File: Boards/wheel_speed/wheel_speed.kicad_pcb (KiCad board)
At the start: 2 copper layers, 38.1 x 50.8 mm, 41 parts, among them J1 CONN_02X03, J2 MM_F_RA_08, U1 MCP2561-E_SN, U101 TPS560430YF, U2 ATMEGA16M1, Y1 Crystal_SMD

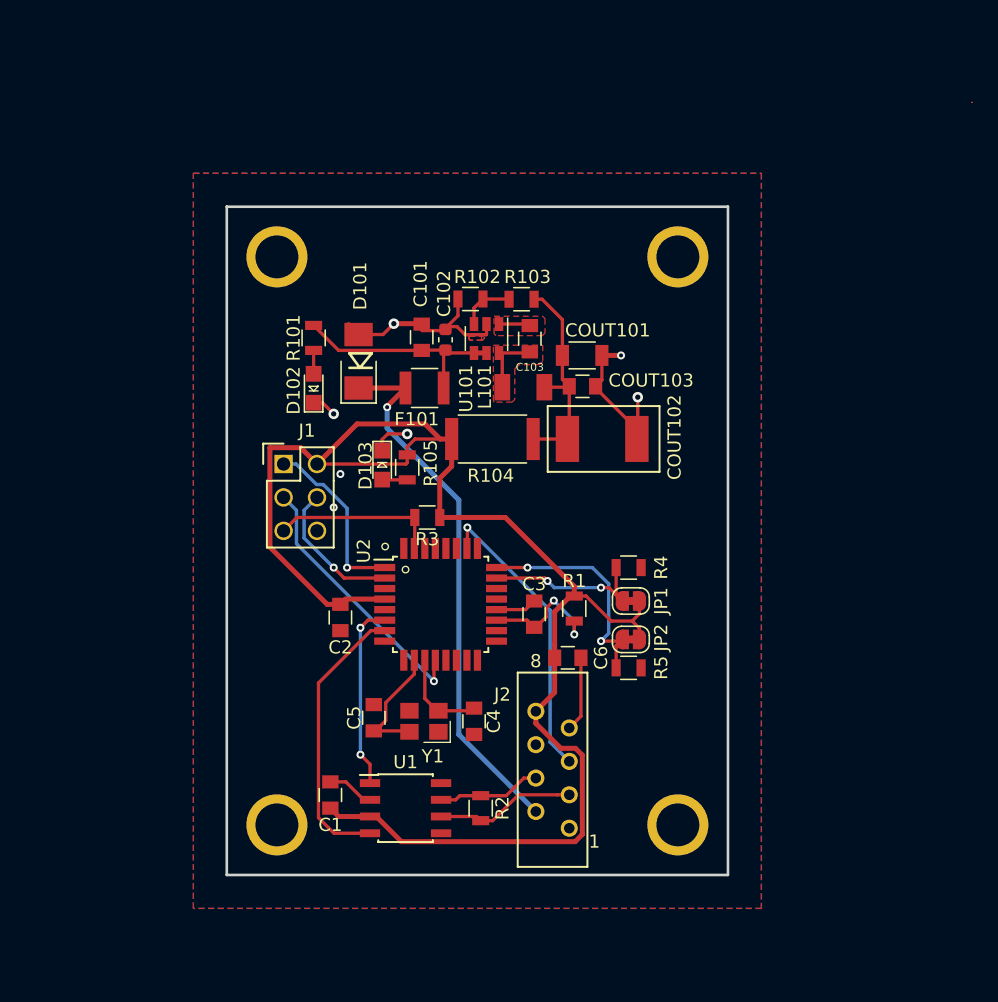
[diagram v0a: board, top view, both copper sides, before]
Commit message: More clear labeling for the jumpers
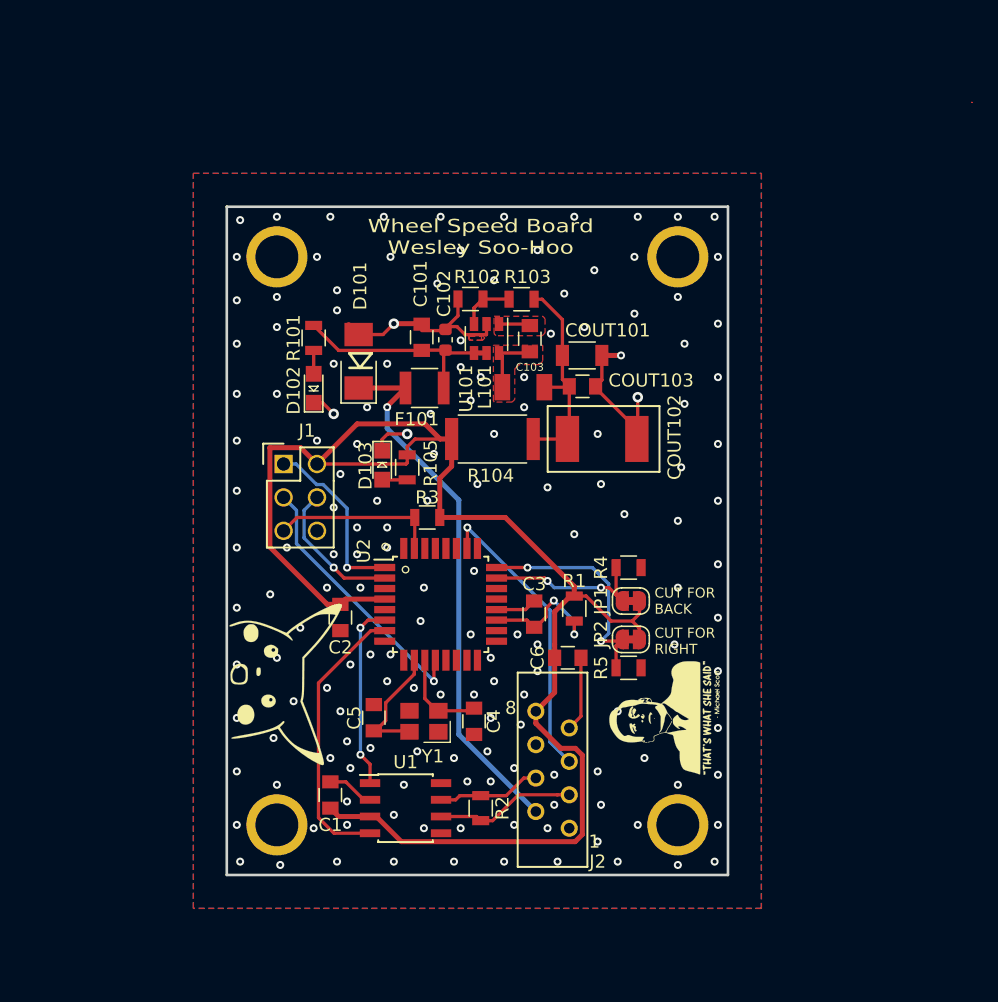
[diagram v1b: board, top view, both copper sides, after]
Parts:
- removed the G*** at (172.7, 91.4)
- added G***: LOGO, img:surprised_pika, F.Cu at (105.4, 112.3)
- added G***: LOGO, img:michael_scott, F.Cu at (134.9, 115.1)
- moved G*** 34.3 mm to (110.0, 100.8), turned to 270 degrees
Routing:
- net GND: vias 7 -> 160
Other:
- board text added: "CUT FOR BACK"
- board text added: "CUT FOR RIGHT"
- board text added: "Wheel Speed Board Wesley Soo-Hoo"

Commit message: Add extra debug lights and redo silkscreen
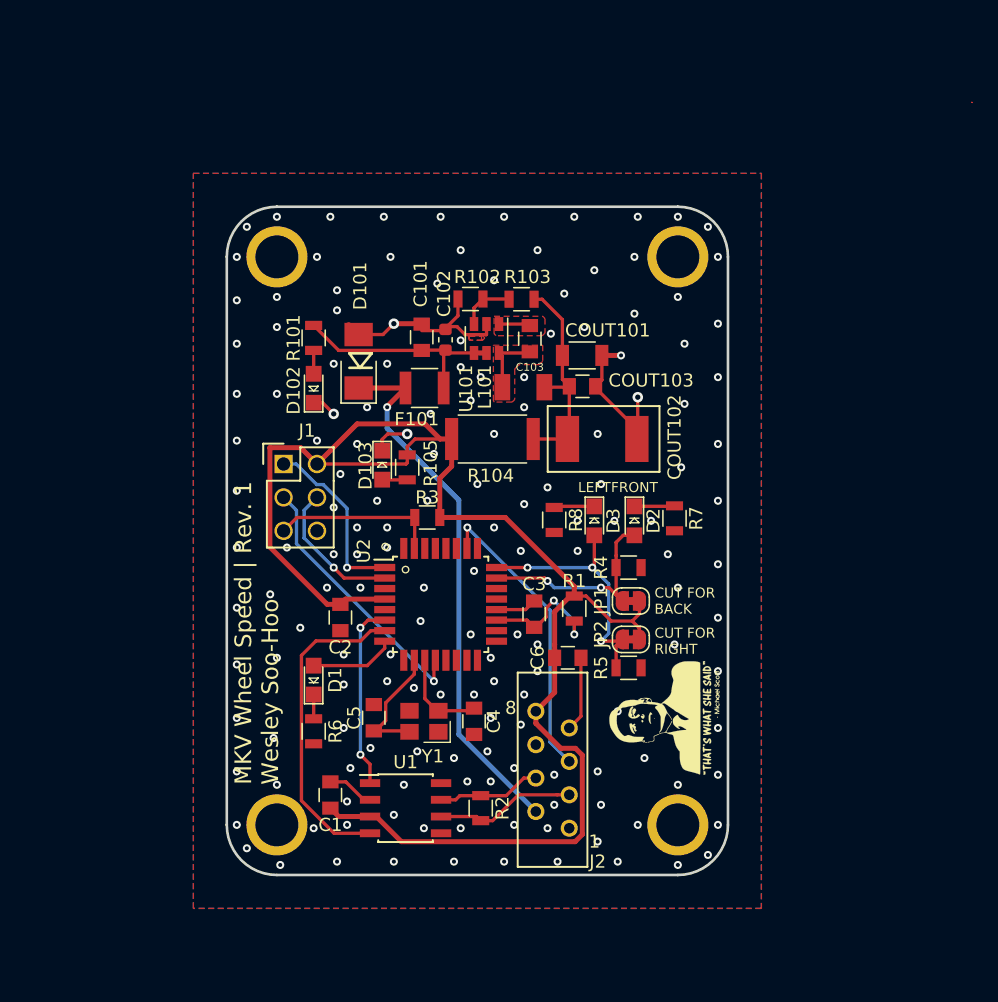
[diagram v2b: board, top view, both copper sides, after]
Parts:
- removed the G*** at (105.4, 112.3)
- added D1: LED_0805, footprints:LED_0805_OEM, F.Cu at (108.2, 112.2)
- added D2: LED_0805, footprints:LED_0805_OEM, F.Cu at (132.6, 100.1)
- added D3: LED_0805, footprints:LED_0805_OEM, F.Cu at (129.5, 100.1)
- added R6: R_120, footprints:R_0805_OEM, F.Cu at (108.2, 116.1)
- added R7: R_120, footprints:R_0805_OEM, F.Cu at (135.6, 99.9)
- added R8: R_120, footprints:R_0805_OEM, F.Cu at (126.5, 100.0)
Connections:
- U2 pad 8: Net-(U2-Pad8) -> /DEBUG
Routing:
- net /DEBUG: track 0.00 -> 6.48 mm
- net /FRONT_SENSE: track 13.0 -> 16.6 mm
- net Net-(D3-Pad1): track 0.00 -> 3.08 mm
- net Net-(D2-Pad1): track 0.00 -> 3.06 mm
- net /CAN_RX: track 21.3 -> 24.4 mm
- net /LEFT_SENSE: track 17.7 -> 20.2 mm, vias 2 -> 3
- net Net-(D1-Pad1): track 0.00 -> 1.84 mm
- net GND: vias 160 -> 161
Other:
- outline, holes or cut-outs redrawn
- board text added: "FRONT"
- board text added: "LEFT"
- board text added: "MKV Wheel Speed | Rev. 1 Wesley Soo-Hoo"
- board text removed: "Wheel Speed Board Wesley Soo-Hoo"

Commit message: fix pinout and move microfit connector to edge of board
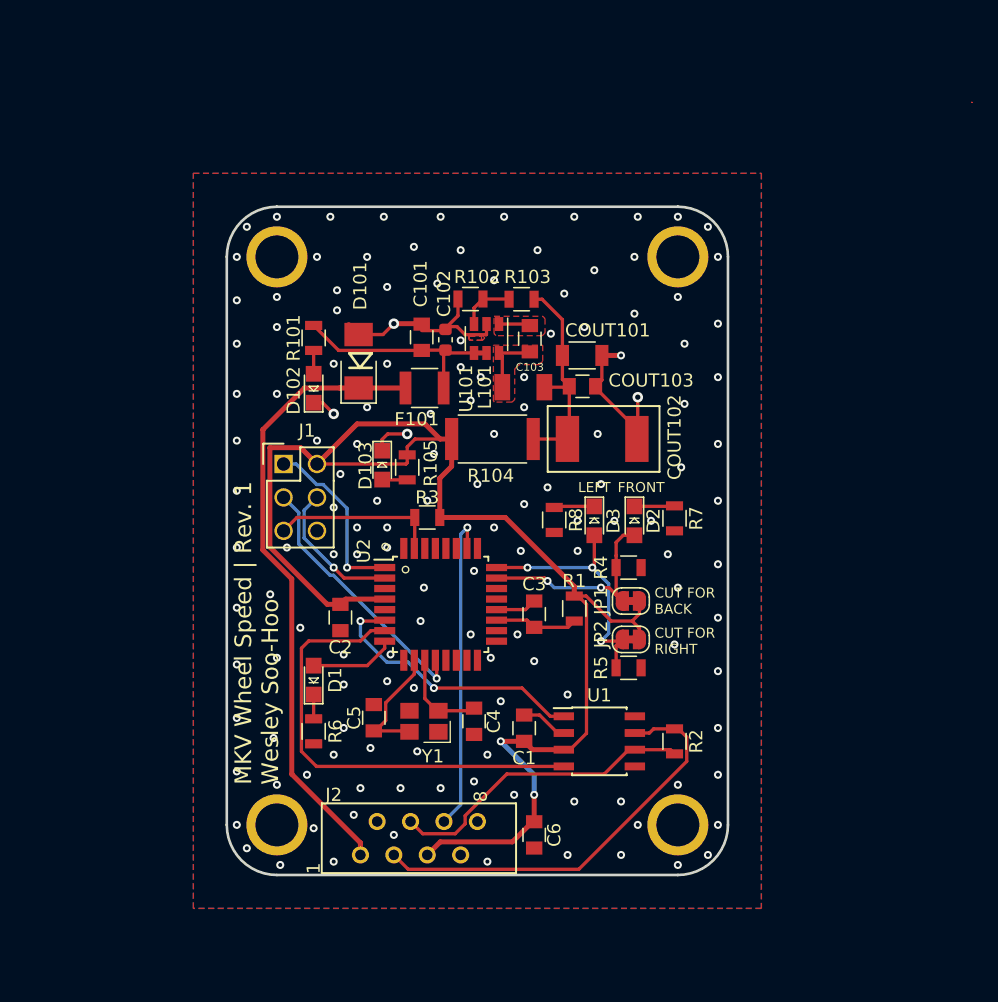
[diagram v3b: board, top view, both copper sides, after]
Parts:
- removed the G*** at (134.9, 115.1)
- moved C1 15.6 mm to (124.2, 115.8)
- moved R2 15.6 mm to (135.6, 116.8)
- moved U1 15.6 mm to (129.9, 116.8)
- moved C6 13.7 mm to (125.0, 124.0), turned to 90 degrees
- moved J2 12.9 mm to (116.8, 125.5), turned to 90 degrees
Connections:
- C6 pad 1: VCC -> GND
- C6 pad 2: GND -> VCC
- J2 pad 1: GND -> /12V
- J2 pad 2: /12V -> GND
- J2 pad 3: /CAN_LO -> /CAN_HI
- J2 pad 4: /CAN_HI -> /CAN_LO
- J2 pad 5: /SENSE_IN -> VCC
- J2 pad 6: GND -> /SENSE_IN
- J2 pad 8: VCC -> GND
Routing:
- net /CAN_HI: track 7.89 -> 32.3 mm
- net /CAN_LO: track 10.7 -> 23.6 mm
- net /CAN_RX: track 24.4 -> 35.1 mm
- net VCC: track 116.5 -> 109.1 mm, vias 0 -> 2
- net /CAN_TX: track 14.2 -> 21.0 mm
- net /12V: track 41.3 -> 47.9 mm, vias 1 -> 0
- net GND: track 44.8 -> 39.1 mm, vias 161 -> 144
- net Net-(C3-Pad1): track 10.0 -> 6.33 mm, vias 2 -> 0
- net /SENSE_IN: track 22.6 -> 24.7 mm

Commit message: Switch to normally open jumpers, rearrange bottom traces
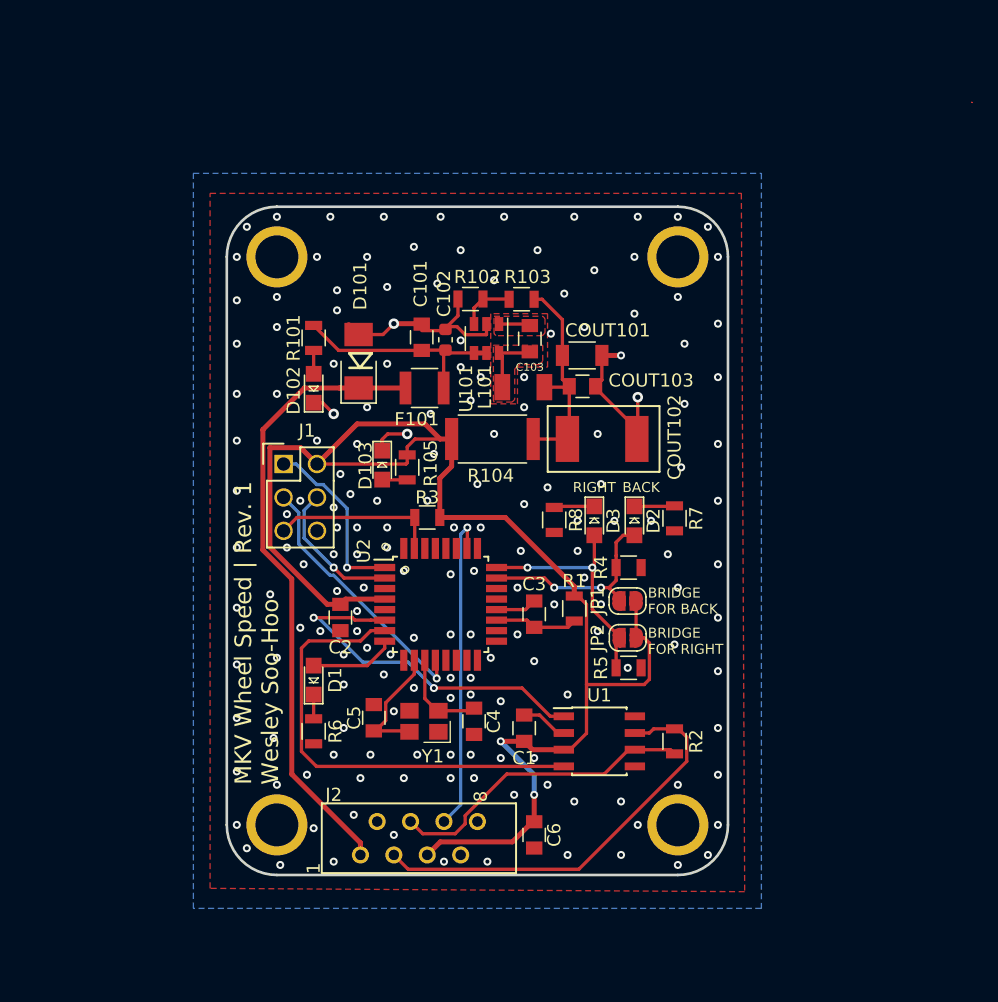
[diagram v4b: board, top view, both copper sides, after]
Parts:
- JP1, JP2: footprint Jumper:SolderJumper-2_P1.3mm_Bridged_RoundedPad1.0x1.5mm -> Jumper:SolderJumper-2_P1.3mm_Open_RoundedPad1.0x1.5mm
- moved JP2 0.27 mm to (132.1, 109.0)
- moved JP1 0.25 mm to (132.1, 106.2)
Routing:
- net /CAN_TX: track 21.0 -> 27.7 mm
- net VCC: track 109.1 -> 112.2 mm
- net /LEFT_SENSE: track 20.2 -> 18.6 mm, vias 3 -> 2
- net /FRONT_SENSE: track 16.6 -> 15.6 mm
- net GND: vias 144 -> 174
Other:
- board text added: "BACK"
- board text added: "BRIDGE FOR BACK"
- board text added: "BRIDGE FOR RIGHT"
- board text added: "RIGHT"
- board text removed: "CUT FOR BACK"
- board text removed: "CUT FOR RIGHT"
- board text removed: "FRONT"
- board text removed: "LEFT"

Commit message: make board outline compatible with the interface board
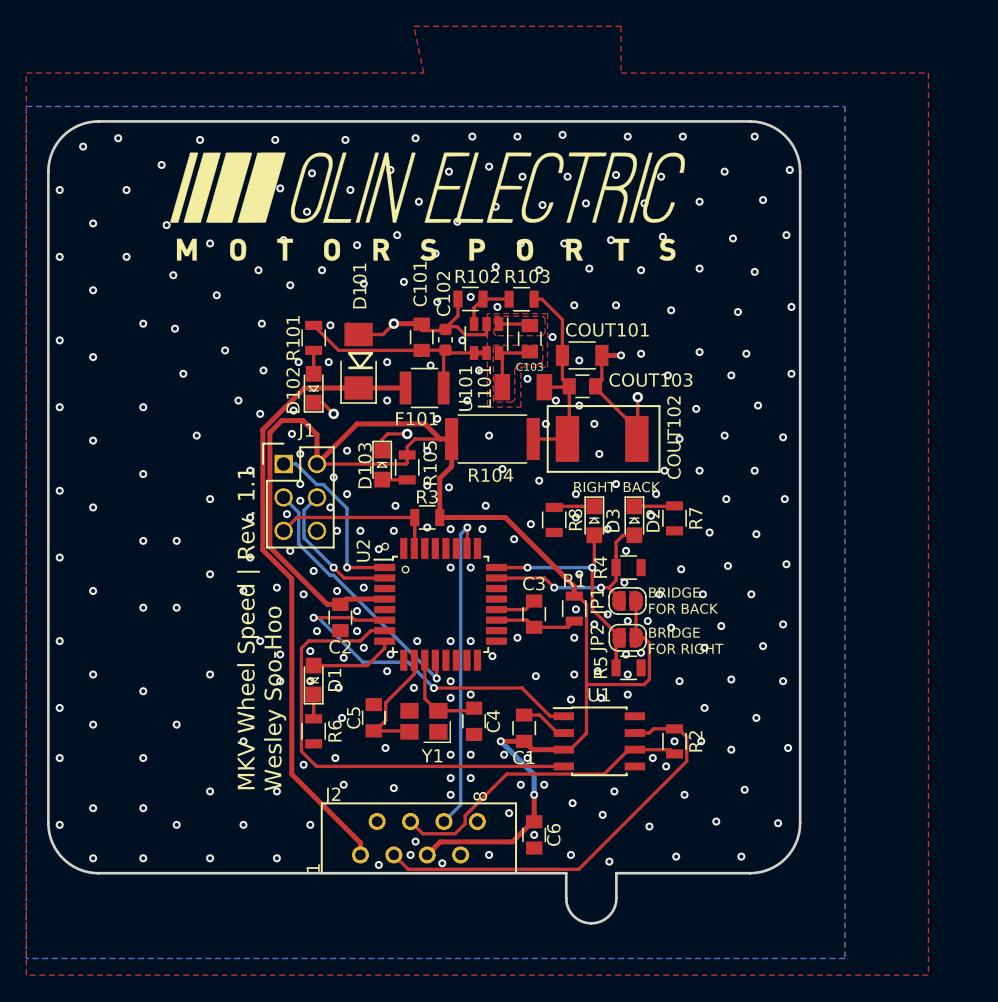
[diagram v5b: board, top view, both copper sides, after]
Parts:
- removed REF** (x4): Mounting_Hole_4-40, footprints:Mounting_Hole_4-40
- added G***: LOGO, footprints:phoenix, B.Cu at (116.8, 97.8)
- G***: moved to F.Cu
- moved G*** 25.6 mm to (116.8, 76.2), turned to 0 degrees
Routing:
- net VCC: track 112.2 -> 115.8 mm
- net GND: vias 174 -> 305
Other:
- board size 38.1 x 50.8 mm -> 57.2 x 61 mm
- board text added: "1"
- board text added: "8"
- board text added: "MKV Wheel Speed | Rev. 1.1 Wesley Soo-Hoo"
- board text removed: "MKV Wheel Speed | Rev. 1 Wesley Soo-Hoo"

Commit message: v0 checklist edits, generate gerbers
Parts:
- moved G*** 32.1 mm to (96.0, 100.6), turned to 90 degrees
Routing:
- net /CAN_LO: track 23.6 -> 22.5 mm
- net /CAN_HI: track 32.3 -> 31.3 mm
- net GND: vias 305 -> 294
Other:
- board text added: "12V PWR"
- board text added: "5V PWR"
- board text added: "DO NOT POPULATE"
- board text added: "MKV Wheel Speed | V0 11/21/2019 Wesley Soo-Hoo"
- board text removed: "MKV Wheel Speed | Rev. 1.1 Wesley Soo-Hoo"

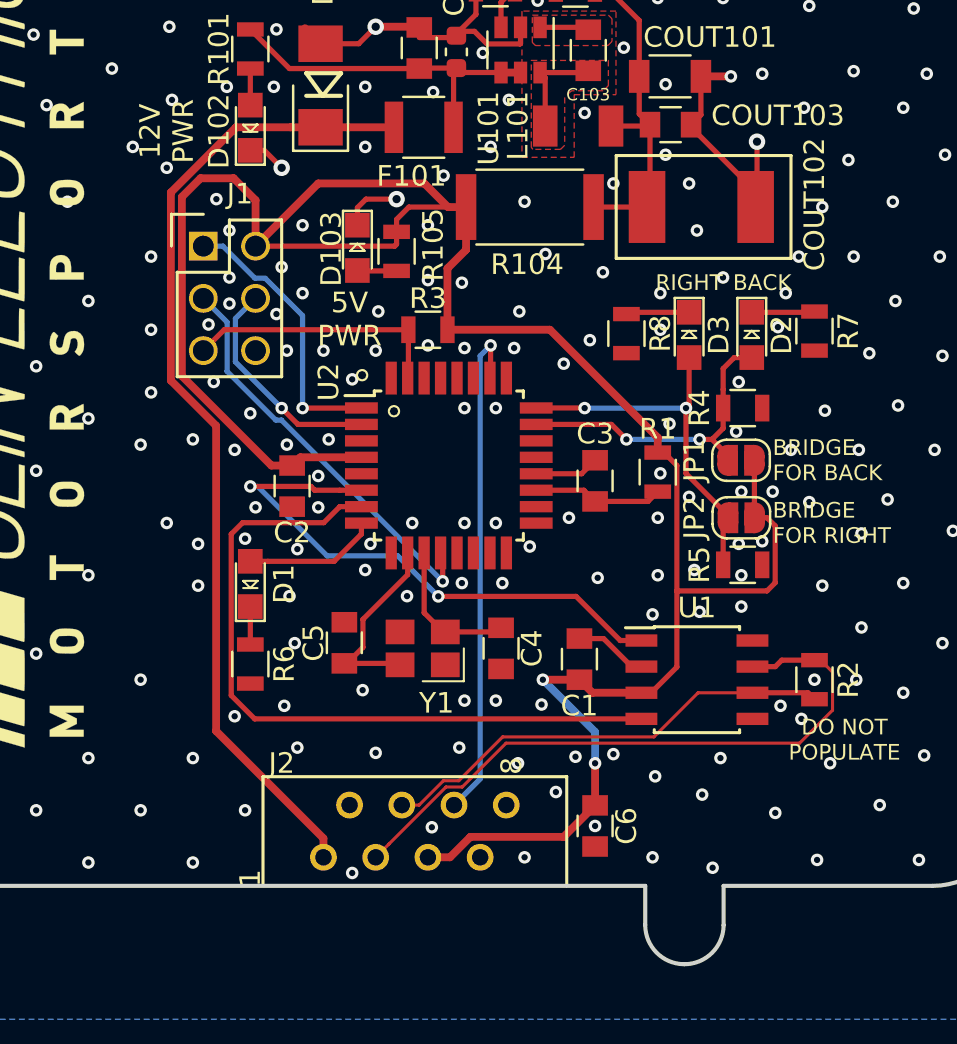
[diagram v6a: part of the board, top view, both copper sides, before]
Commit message: rotate connector 180 degrees
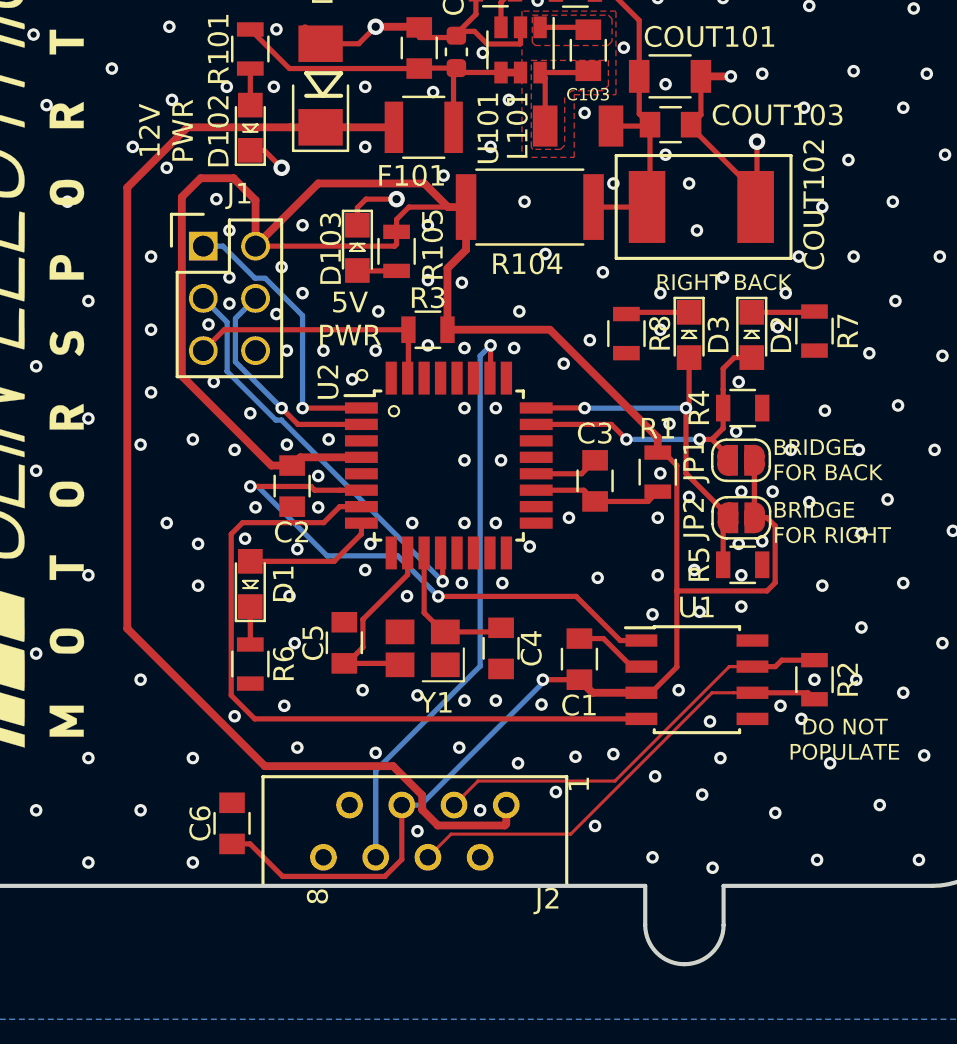
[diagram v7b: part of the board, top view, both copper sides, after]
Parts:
- moved C6 17.7 mm to (107.3, 123.8), turned to 270 degrees
- moved J2 2.84 mm to (115.6, 122.9), turned to 270 degrees
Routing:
- net /12V: track 47.9 -> 59.7 mm
- net /CAN_HI: track 31.3 -> 20.4 mm
- net VCC: track 115.8 -> 120.9 mm, vias 2 -> 1
- net /SENSE_IN: track 24.7 -> 28.8 mm
- net GND: vias 294 -> 297
